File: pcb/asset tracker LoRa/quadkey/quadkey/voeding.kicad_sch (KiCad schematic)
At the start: 15 parts, among them U1 MCP73831, U2 TPS63001, con1 USB_micro

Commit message: 34t
34t
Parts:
- removed con1: USB_micro, connectors_user:usb_connector, symbol conectors:USB_micro
- added J1: USB_B_Mini, connectors_user:AMPHENOL_10118192-0001LF, symbol Connector:USB_B_Mini
- L2: footprint vanalles:INDM300X300X200L80X50 -> vanalles:WURTH_744025001
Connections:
- net GND: now also J1.5 (GND), J1.6 (Shield)
- net at L1.1: now also J1.1 (VBUS)
- no-connect marks 7 -> 5
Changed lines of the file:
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@@
     (comment 1 "bopla behuizing 34111511")
   )
+  (junction (at 43.18 63.5) (diameter 0.9144) (color 0 0 0 0))
   (junction (at 92.71 127) (diameter 0.9144) (color 0 0 0 0))
   (junction (at 104.14 29.21) (diameter 0.9144) (color 0 0 0 0))
@@
   (junction (at 196.85 127) (diameter 0.9144) (color 0 0 0 0))
   (no_connect (at 39.37 39.37))
-  (no_connect (at 39.37 57.15))
   (no_connect (at 43.18 39.37))
-  (no_connect (at 43.18 57.15))
-  (no_connect (at 52.07 45.72))
   (no_connect (at 52.07 48.26))
   (no_connect (at 52.07 50.8))
+  (no_connect (at 52.07 53.34))
   (wire (pts (xy 40.64 123.19) (xy 40.64 127))
     (stroke (width 0) (type solid) (color 0 0 0 0))
@@
     (stroke (width 0) (type solid) (color 0 0 0 0))
   )
-  (wire (pts (xy 53.34 53.34) (xy 52.07 53.34))
-    (stroke (width 0) (type solid) (color 0 0 0 0))
-  )
-  (wire (pts (xy 53.34 57.15) (xy 53.34 53.34))
+  (wire (pts (xy 41.91 63.5) (xy 41.91 58.42))
+    (stroke (width 0) (type solid) (color 0 0 0 0))
+  )
+  (wire (pts (xy 43.18 63.5) (xy 41.91 63.5))
+    (stroke (width 0) (type solid) (color 0 0 0 0))
+  )
+  (wire (pts (xy 44.45 58.42) (xy 44.45 63.5))
+    (stroke (width 0) (type solid) (color 0 0 0 0))
+  )
+  (wire (pts (xy 44.45 63.5) (xy 43.18 63.5))
     (stroke (width 0) (type solid) (color 0 0 0 0))
   )
@@
   (symbol (lib_id "power:vbat") (at 40.64 123.19 0) (unit 1)
     (in_bom no) (on_board no)
-    (property "Reference" "vbat?" (id 0) (at 44.45 121.92 0)
+    (property "Reference" "#vbat0101" (id 0) (at 44.45 121.92 0)
       (effects (font (size 1.27 1.27)) hide)
     )
@@
   (symbol (lib_id "power:vbat") (at 92.71 120.65 0) (unit 1)
     (in_bom no) (on_board no)
-    (property "Reference" "vbat?" (id 0) (at 96.52 119.38 0)
+    (property "Reference" "#vbat0102" (id 0) (at 96.52 119.38 0)
       (effects (font (size 1.27 1.27)) hide)
     )
@@
   (symbol (lib_id "power:vbat") (at 162.56 21.59 0) (unit 1)
     (in_bom no) (on_board no)
-    (property "Reference" "vbat?" (id 0) (at 166.37 20.32 0)
+    (property "Reference" "#vbat0103" (id 0) (at 166.37 20.32 0)
       (effects (font (size 1.27 1.27)) hide)
     )
@@
     (pin "1")
   )
-  (symbol (lib_id "power:GND") (at 53.34 57.15 0) (unit 1)
-    (in_bom yes) (on_board yes) (fields_autoplaced)
-    (property "Reference" "#PWR0104" (id 0) (at 53.34 63.5 0)
-      (effects (font (size 1.27 1.27)) hide)
-    )
-    (property "Value" "GND" (id 1) (at 53.34 62.23 0))
-    (property "Footprint" "" (id 2) (at 53.34 57.15 0)
-      (effects (font (size 1.27 1.27)) hide)
-    )
-    (property "Datasheet" "" (id 3) (at 53.34 57.15 0)
+  (symbol (lib_id "power:GND") (at 43.18 63.5 0) (unit 1)
+    (in_bom yes) (on_board yes) (fields_autoplaced)
+    (property "Reference" "#PWR0104" (id 0) (at 43.18 69.85 0)
+      (effects (font (size 1.27 1.27)) hide)
+    )
+    (property "Value" "GND" (id 1) (at 43.18 68.58 0))
+    (property "Footprint" "" (id 2) (at 43.18 63.5 0)
+      (effects (font (size 1.27 1.27)) hide)
+    )
+    (property "Datasheet" "" (id 3) (at 43.18 63.5 0)
       (effects (font (size 1.27 1.27)) hide)
     )
@@
     (property "Reference" "L2" (id 0) (at 146.05 102.87 90))
     (property "Value" "2.2uH" (id 1) (at 146.05 105.41 90))
-    (property "Footprint" "vanalles:INDM300X300X200L80X50" (id 2) (at 146.05 107.95 0)
+    (property "Footprint" "vanalles:WURTH_744025001" (id 2) (at 146.05 107.95 0)
       (effects (font (size 1.27 1.27)) hide)
     )
@@
     (pin "5")
   )
-  (symbol (lib_id "conectors:USB_micro") (at 49.53 43.18 0) (mirror y) (unit 1)
-    (in_bom yes) (on_board yes) (fields_autoplaced)
-    (property "Reference" "con1" (id 0) (at 36.83 47.6249 0)
-      (effects (font (size 1.27 1.27)) (justify left))
-    )
-    (property "Value" "USB_micro" (id 1) (at 36.83 50.1649 0)
-      (effects (font (size 1.27 1.27)) (justify left))
-    )
-    (property "Footprint" "connectors_user:usb_connector" (id 2) (at 49.53 43.18 0)
-      (effects (font (size 1.27 1.27)) hide)
-    )
-    (property "Datasheet" "" (id 3) (at 49.53 43.18 0)
+  (symbol (lib_id "Connector:USB_B_Mini") (at 44.45 48.26 0) (unit 1)
+    (in_bom yes) (on_board yes) (fields_autoplaced)
+    (property "Reference" "J1" (id 0) (at 45.847 36.83 0))
+    (property "Value" "USB_B_Mini" (id 1) (at 45.847 39.37 0))
+    (property "Footprint" "connectors_user:AMPHENOL_10118192-0001LF" (id 2) (at 48.26 49.53 0)
+      (effects (font (size 1.27 1.27)) hide)
+    )
+    (property "Datasheet" "" (id 3) (at 48.26 49.53 0)
       (effects (font (size 1.27 1.27)) hide)
     )
@@
     (pin "5")
     (pin "6")
-    (pin "7")
-    (pin "8")
-    (pin "9")
   )
   (symbol (lib_id "Regulator_Switching:TPS63001") (at 146.05 132.08 0) (unit 1)

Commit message: code
code
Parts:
- removed J1: USB_B_Mini, connectors_user:AMPHENOL_10118192-0001LF, symbol Connector:USB_B_Mini
- added con1: USB_micro, connectors_user:MILLMAX_897-43-005-00-100001, symbol conectors:USB_micro
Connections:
- net GND: now also con1.5 (GND), con1.6, con1.7, con1.8, con1.9
- net at L1.1: now also con1.1 (VBUS)
- no-connect marks 5 -> 3
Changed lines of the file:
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@@
     (comment 1 "bopla behuizing 34111511")
   )
-  (junction (at 43.18 63.5) (diameter 0.9144) (color 0 0 0 0))
+  (junction (at 39.37 38.1) (diameter 0.9144) (color 0 0 0 0))
+  (junction (at 39.37 57.15) (diameter 0.9144) (color 0 0 0 0))
+  (junction (at 43.18 57.15) (diameter 0.9144) (color 0 0 0 0))
+  (junction (at 46.99 57.15) (diameter 0.9144) (color 0 0 0 0))
+  (junction (at 48.26 62.23) (diameter 0.9144) (color 0 0 0 0))
+  (junction (at 49.53 57.15) (diameter 0.9144) (color 0 0 0 0))
   (junction (at 92.71 127) (diameter 0.9144) (color 0 0 0 0))
   (junction (at 104.14 29.21) (diameter 0.9144) (color 0 0 0 0))
@@
   (junction (at 190.5 147.32) (diameter 0.9144) (color 0 0 0 0))
   (junction (at 196.85 127) (diameter 0.9144) (color 0 0 0 0))
-  (no_connect (at 39.37 39.37))
-  (no_connect (at 43.18 39.37))
+  (no_connect (at 52.07 45.72))
   (no_connect (at 52.07 48.26))
   (no_connect (at 52.07 50.8))
-  (no_connect (at 52.07 53.34))
+  (wire (pts (xy 24.13 38.1) (xy 24.13 57.15))
+    (stroke (width 0) (type solid) (color 0 0 0 0))
+  )
+  (wire (pts (xy 24.13 57.15) (xy 39.37 57.15))
+    (stroke (width 0) (type solid) (color 0 0 0 0))
+  )
+  (wire (pts (xy 39.37 38.1) (xy 24.13 38.1))
+    (stroke (width 0) (type solid) (color 0 0 0 0))
+  )
+  (wire (pts (xy 39.37 38.1) (xy 43.18 38.1))
+    (stroke (width 0) (type solid) (color 0 0 0 0))
+  )
+  (wire (pts (xy 39.37 39.37) (xy 39.37 38.1))
+    (stroke (width 0) (type solid) (color 0 0 0 0))
+  )
   (wire (pts (xy 40.64 123.19) (xy 40.64 127))
     (stroke (width 0) (type solid) (color 0 0 0 0))
@@
     (stroke (width 0) (type solid) (color 0 0 0 0))
   )
-  (wire (pts (xy 41.91 63.5) (xy 41.91 58.42))
-    (stroke (width 0) (type solid) (color 0 0 0 0))
-  )
-  (wire (pts (xy 43.18 63.5) (xy 41.91 63.5))
-    (stroke (width 0) (type solid) (color 0 0 0 0))
-  )
-  (wire (pts (xy 44.45 58.42) (xy 44.45 63.5))
-    (stroke (width 0) (type solid) (color 0 0 0 0))
-  )
-  (wire (pts (xy 44.45 63.5) (xy 43.18 63.5))
+  (wire (pts (xy 43.18 39.37) (xy 43.18 38.1))
+    (stroke (width 0) (type solid) (color 0 0 0 0))
+  )
+  (wire (pts (xy 43.18 57.15) (xy 39.37 57.15))
+    (stroke (width 0) (type solid) (color 0 0 0 0))
+  )
+  (wire (pts (xy 46.99 57.15) (xy 43.18 57.15))
+    (stroke (width 0) (type solid) (color 0 0 0 0))
+  )
+  (wire (pts (xy 46.99 62.23) (xy 46.99 57.15))
+    (stroke (width 0) (type solid) (color 0 0 0 0))
+  )
+  (wire (pts (xy 48.26 62.23) (xy 46.99 62.23))
+    (stroke (width 0) (type solid) (color 0 0 0 0))
+  )
+  (wire (pts (xy 49.53 57.15) (xy 46.99 57.15))
+    (stroke (width 0) (type solid) (color 0 0 0 0))
+  )
+  (wire (pts (xy 49.53 57.15) (xy 49.53 62.23))
+    (stroke (width 0) (type solid) (color 0 0 0 0))
+  )
+  (wire (pts (xy 49.53 62.23) (xy 48.26 62.23))
+    (stroke (width 0) (type solid) (color 0 0 0 0))
+  )
+  (wire (pts (xy 52.07 53.34) (xy 53.34 53.34))
+    (stroke (width 0) (type solid) (color 0 0 0 0))
+  )
+  (wire (pts (xy 53.34 53.34) (xy 53.34 57.15))
+    (stroke (width 0) (type solid) (color 0 0 0 0))
+  )
+  (wire (pts (xy 53.34 57.15) (xy 49.53 57.15))
     (stroke (width 0) (type solid) (color 0 0 0 0))
   )
@@
     (pin "1")
   )
-  (symbol (lib_id "power:GND") (at 43.18 63.5 0) (unit 1)
-    (in_bom yes) (on_board yes) (fields_autoplaced)
-    (property "Reference" "#PWR0104" (id 0) (at 43.18 69.85 0)
-      (effects (font (size 1.27 1.27)) hide)
-    )
-    (property "Value" "GND" (id 1) (at 43.18 68.58 0))
-    (property "Footprint" "" (id 2) (at 43.18 63.5 0)
-      (effects (font (size 1.27 1.27)) hide)
-    )
-    (property "Datasheet" "" (id 3) (at 43.18 63.5 0)
+  (symbol (lib_id "power:GND") (at 48.26 62.23 0) (unit 1)
+    (in_bom yes) (on_board yes) (fields_autoplaced)
+    (property "Reference" "#PWR0104" (id 0) (at 48.26 68.58 0)
+      (effects (font (size 1.27 1.27)) hide)
+    )
+    (property "Value" "GND" (id 1) (at 48.26 67.31 0))
+    (property "Footprint" "" (id 2) (at 48.26 62.23 0)
+      (effects (font (size 1.27 1.27)) hide)
+    )
+    (property "Datasheet" "" (id 3) (at 48.26 62.23 0)
       (effects (font (size 1.27 1.27)) hide)
     )
@@
     (pin "5")
   )
-  (symbol (lib_id "Connector:USB_B_Mini") (at 44.45 48.26 0) (unit 1)
-    (in_bom yes) (on_board yes) (fields_autoplaced)
-    (property "Reference" "J1" (id 0) (at 45.847 36.83 0))
-    (property "Value" "USB_B_Mini" (id 1) (at 45.847 39.37 0))
-    (property "Footprint" "connectors_user:AMPHENOL_10118192-0001LF" (id 2) (at 48.26 49.53 0)
-      (effects (font (size 1.27 1.27)) hide)
-    )
-    (property "Datasheet" "" (id 3) (at 48.26 49.53 0)
+  (symbol (lib_id "conectors:USB_micro") (at 49.53 43.18 0) (mirror y) (unit 1)
+    (in_bom yes) (on_board yes) (fields_autoplaced)
+    (property "Reference" "con1" (id 0) (at 36.83 47.6249 0)
+      (effects (font (size 1.27 1.27)) (justify left))
+    )
+    (property "Value" "USB_micro" (id 1) (at 36.83 50.1649 0)
+      (effects (font (size 1.27 1.27)) (justify left))
+    )
+    (property "Footprint" "connectors_user:MILLMAX_897-43-005-00-100001" (id 2) (at 49.53 43.18 0)
+      (effects (font (size 1.27 1.27)) hide)
+    )
+    (property "Datasheet" "" (id 3) (at 49.53 43.18 0)
       (effects (font (size 1.27 1.27)) hide)
     )
@@
     (pin "5")
     (pin "6")
+    (pin "7")
+    (pin "8")
+    (pin "9")
   )
   (symbol (lib_id "Regulator_Switching:TPS63001") (at 146.05 132.08 0) (unit 1)

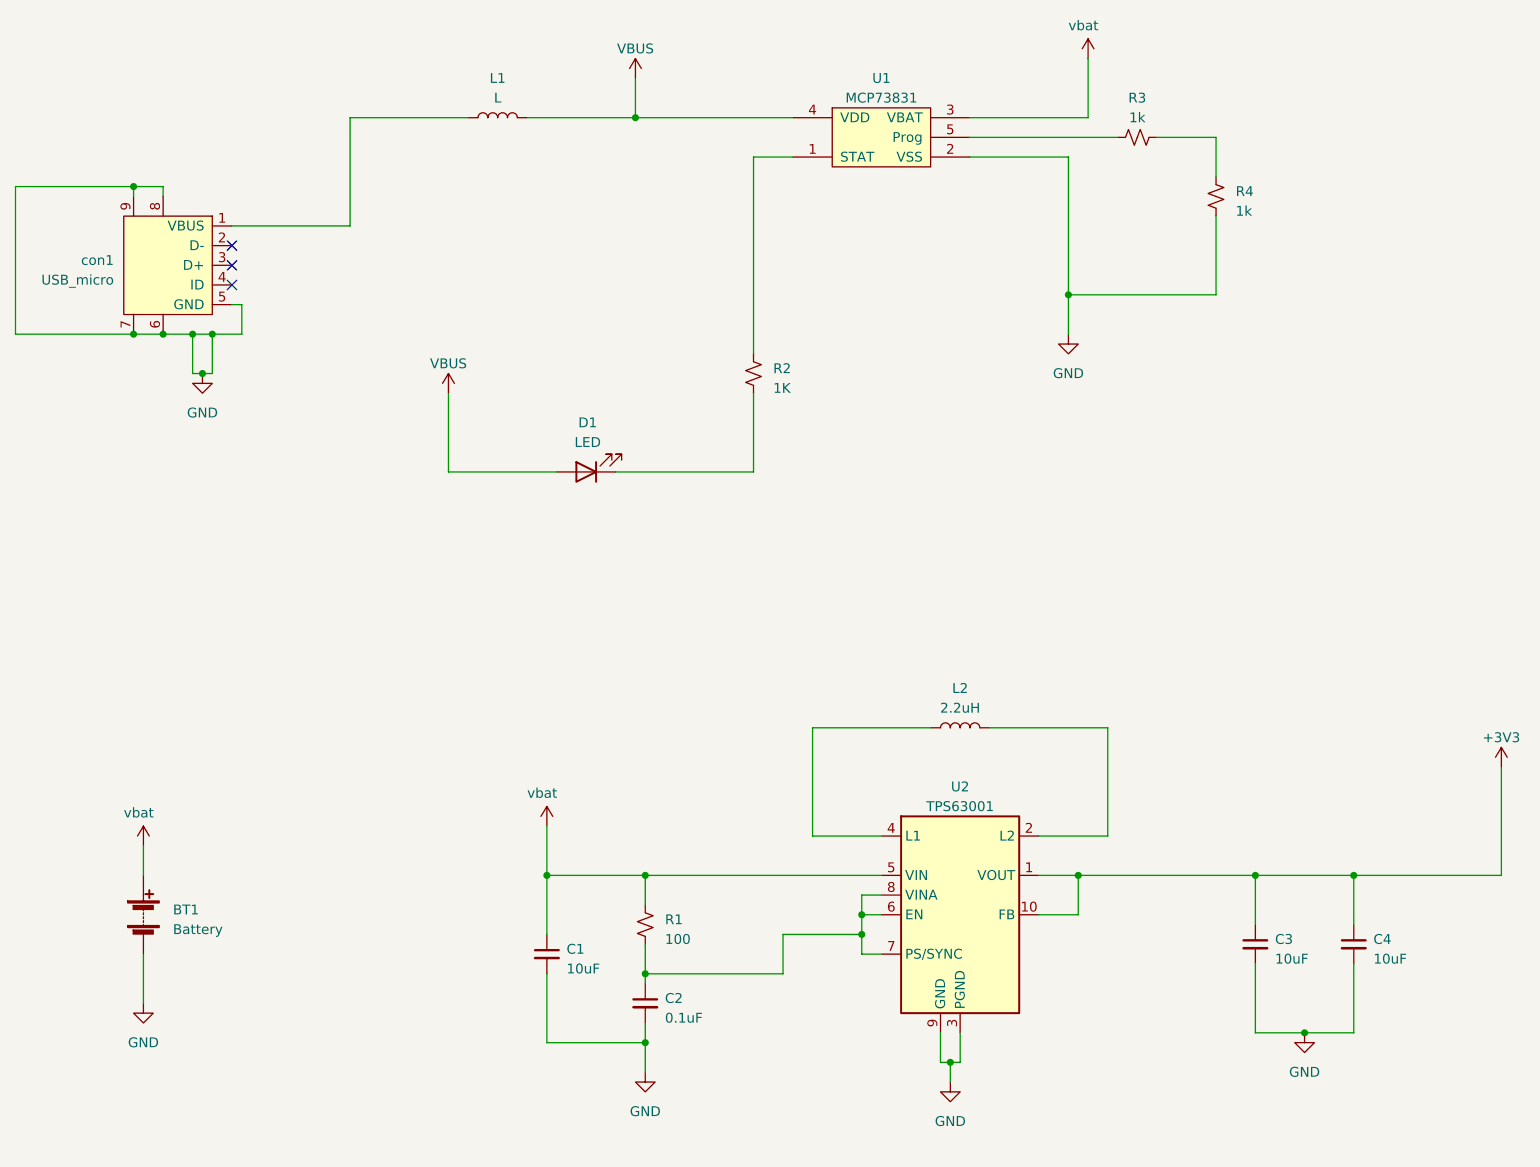
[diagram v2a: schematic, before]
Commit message: versie2
aan versie 2 begonnen met tekenen en code beginnen schrijven voor quadkey
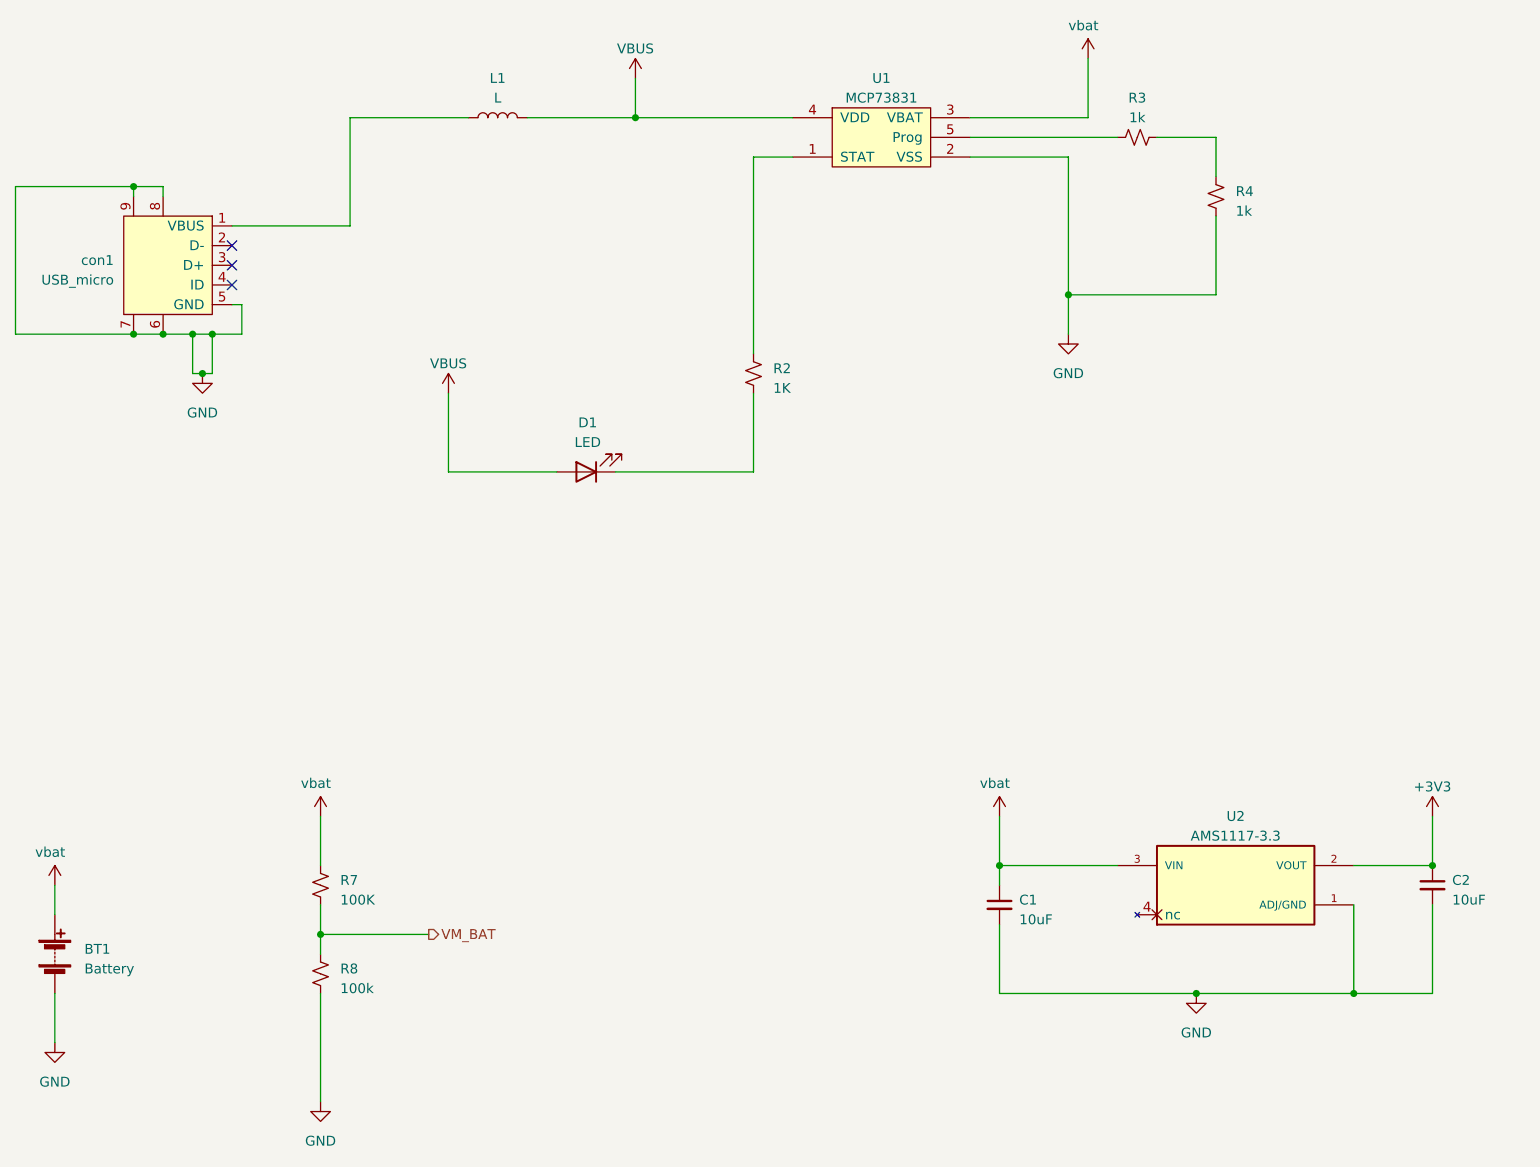
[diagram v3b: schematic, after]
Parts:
- removed C3, C4: 10uF, vanalles:0603, symbol Device:C_Small
- removed L2: 2.2uH, vanalles:WURTH_744025001, symbol Device:L
- removed R1: 100, vanalles:0603RL, symbol Device:R_Small_US
- removed U2: TPS63001, halfgeleiders:SON50P300X300X100-11N, symbol Regulator_Switching:TPS63001
- added R7: 100K, vanalles:0603RL, symbol Device:R_Small_US
- added R8: 100k, vanalles:0603RL, symbol Device:R_Small_US
- added U2: AMS1117-3.3, halfgeleiders:SOT229P700X180-4N, symbol AMS1117-3.3:AMS1117-3.3
- C2: value 0.1uF -> 10uF
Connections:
- net +3V3: now also C2.1, U2.2 (VOUT)
- net GND: now also R8.1, U2.1 (ADJ/GND)
- net VBAT: now also R7.2, U2.3 (VIN)
- new net VM_BAT: R7.1, R8.2
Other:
- moved on the sheet: BT1, C1
